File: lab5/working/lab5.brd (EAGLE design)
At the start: 133.9 x 134 mm, 52 parts, among them J1 ISP, Q1 FET, Q2 FET, Q3 FET, Q4 FET, U1 ATMEGA128RFA1, Y1 16MHz

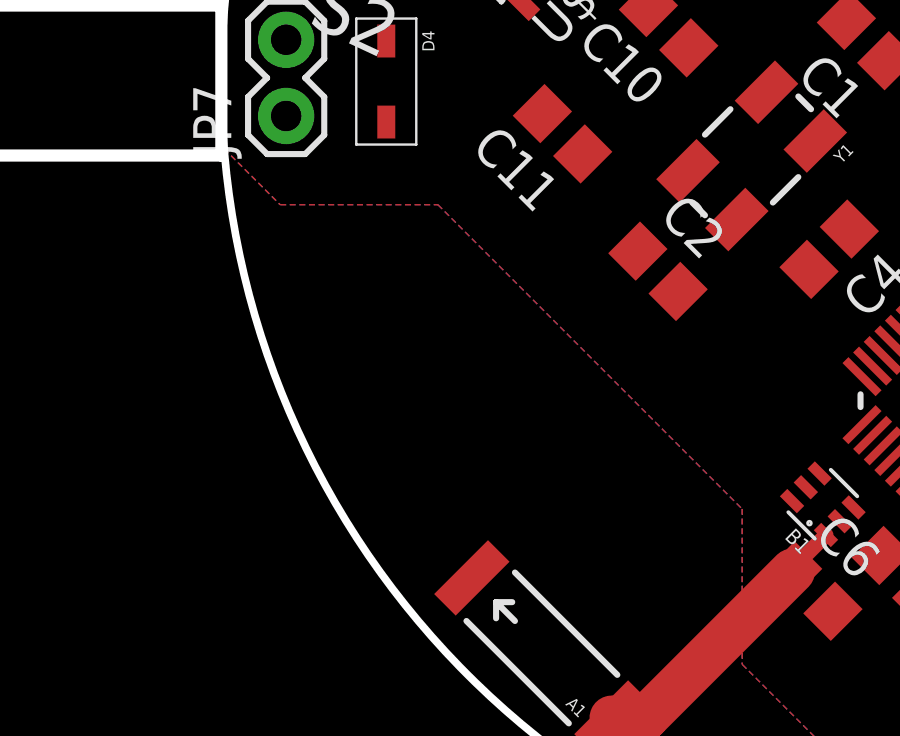
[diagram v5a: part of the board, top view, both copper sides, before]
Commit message: added logo to board
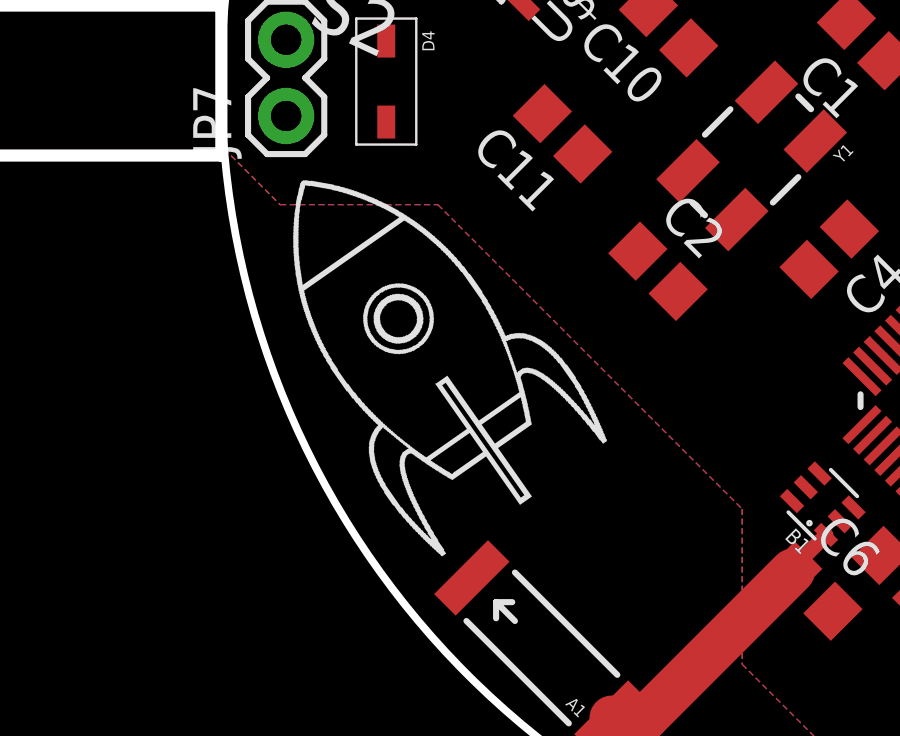
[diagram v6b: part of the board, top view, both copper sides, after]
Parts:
- added U$3: (no value), lab4:ROCKET_LOGO
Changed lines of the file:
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@@
 </element>
 <element name="C5" library="Lab5" package="C0805" value="1 uF" x="9.12498125" y="-7.389125" rot="R135"/>
+<element name="U$3" library="lab4" package="ROCKET_LOGO" value="" x="-20.88895625" y="-16.123996875" rot="R35"/>
 </elements>
 <signals>

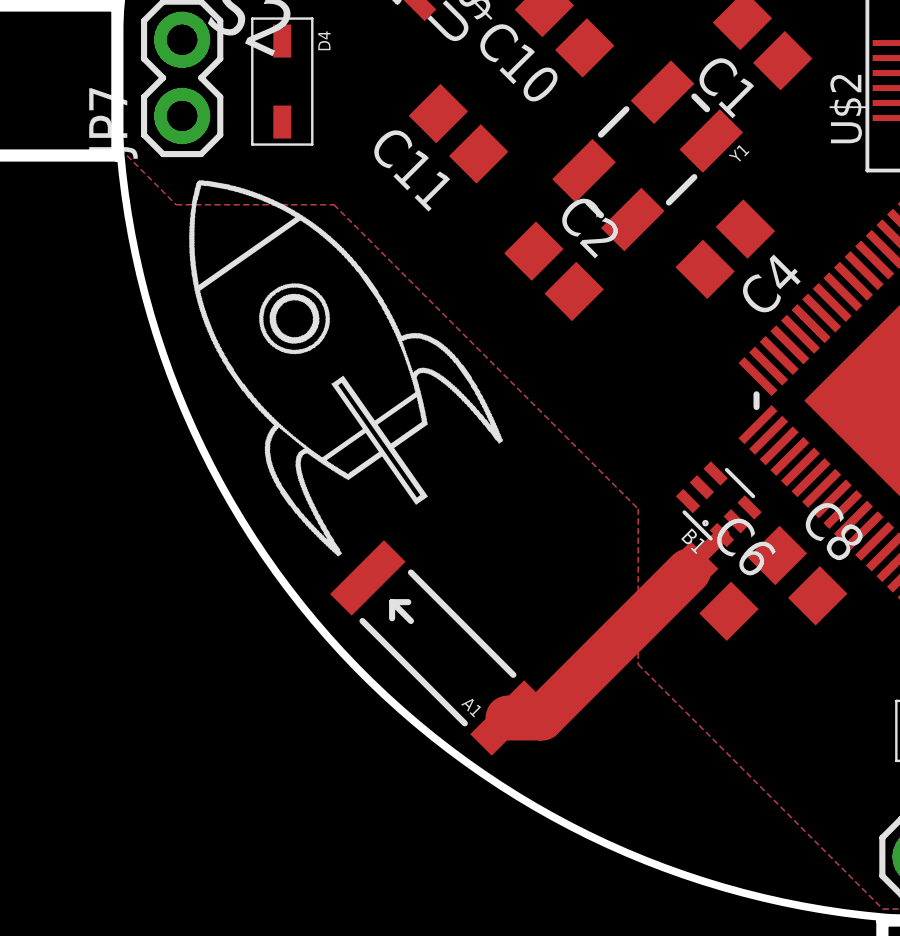
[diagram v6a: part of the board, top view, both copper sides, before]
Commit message: updated radio, moved antenna closer
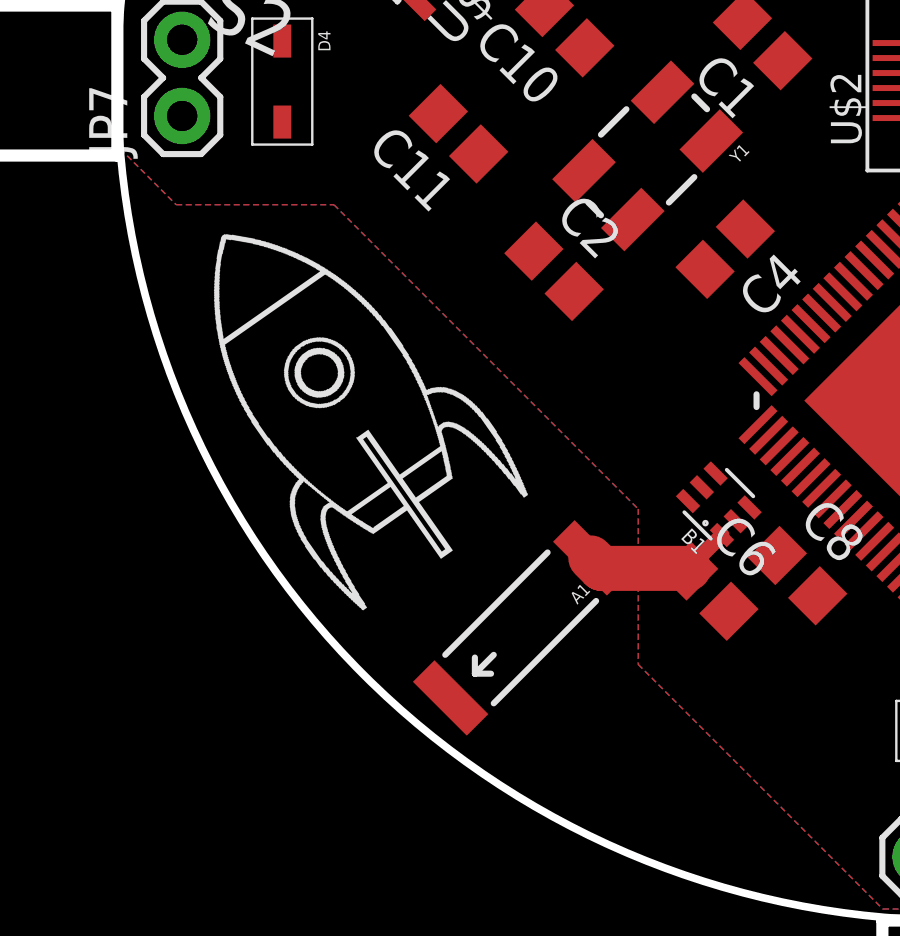
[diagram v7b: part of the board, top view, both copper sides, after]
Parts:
- moved A1 2.84 mm to (-14.6, -18.2), turned to 225 degrees
- moved U$3 1.98 mm to (-20.1, -17.9)
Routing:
- net N$4: track 9.71 -> 5.07 mm
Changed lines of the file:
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@@
 </polygon>
 <wire x1="66.72900625" y1="-0.255303125" x2="66.72900625" y2="0.244696875" width="0.4064" layer="20"/>
+<rectangle x1="-1.32" y1="-1.44" x2="1.32" y2="1.38" layer="41"/>
+<rectangle x1="-1.26" y1="-1.44" x2="1.32" y2="1.38" layer="42"/>
+<rectangle x1="-1.2" y1="-1.32" x2="1.32" y2="1.38" layer="43"/>
+<wire x1="-26.89" y1="-4.53" x2="-21.39" y2="-4.53" width="0.4" layer="39"/>
+<wire x1="-21.39" y1="-4.53" x2="-12.28" y2="-13.64" width="0.4" layer="39"/>
+<wire x1="-12.28" y1="-13.64" x2="-12.44" y2="-13.64" width="0.4" layer="39"/>
+<wire x1="-12.44" y1="-13.64" x2="-18.52" y2="-19.72" width="0.4" layer="39"/>
+<wire x1="-18.52" y1="-19.72" x2="-22.7" y2="-15.54" width="0.4" layer="39"/>
+<wire x1="-22.7" y1="-15.54" x2="-22.7" y2="-13.87" width="0.4" layer="39"/>
+<wire x1="-22.7" y1="-13.87" x2="-24.91" y2="-11.66" width="0.4" layer="39"/>
+<wire x1="-24.91" y1="-11.66" x2="-24.91" y2="-7.56" width="0.4" layer="39"/>
+<wire x1="-24.91" y1="-7.56" x2="-26.89" y2="-5.58" width="0.4" layer="39"/>
+<wire x1="-26.89" y1="-5.58" x2="-26.89" y2="-4.46" width="0.4" layer="39"/>
+<wire x1="-26.89" y1="-4.46" x2="-26.93" y2="-4.42" width="0.4" layer="39"/>
+<wire x1="-26.93" y1="-4.42" x2="-27" y2="-4.42" width="0.4" layer="39"/>
+<wire x1="-11.78" y1="-18.02" x2="-15.53" y2="-21.77" width="0.4" layer="39"/>
+<wire x1="-15.53" y1="-21.77" x2="-15.53" y2="-22.01" width="0.4" layer="39"/>
+<wire x1="-15.53" y1="-22.01" x2="-13.21" y2="-24.33" width="0.4" layer="39"/>
+<wire x1="-13.21" y1="-24.33" x2="-12.44" y2="-24.33" width="0.4" layer="39"/>
+<wire x1="-12.44" y1="-24.33" x2="-11.78" y2="-24.99" width="0.4" layer="39"/>
+<wire x1="-11.78" y1="-24.99" x2="-10.03" y2="-24.99" width="0.4" layer="39"/>
+<wire x1="-10.03" y1="-24.99" x2="-8.91" y2="-26.11" width="0.4" layer="39"/>
+<wire x1="-8.91" y1="-26.11" x2="-7.28" y2="-26.11" width="0.4" layer="39"/>
+<wire x1="-7.28" y1="-26.11" x2="-7.08" y2="-26.31" width="0.4" layer="39"/>
+<wire x1="-7.08" y1="-26.31" x2="-4.53" y2="-26.31" width="0.4" layer="39"/>
+<wire x1="-4.53" y1="-26.31" x2="-11.78" y2="-19.06" width="0.4" layer="39"/>
+<wire x1="-11.78" y1="-19.06" x2="-11.78" y2="-17.94" width="0.4" layer="39"/>
+<wire x1="-26.89" y1="-4.46" x2="-25.26" y2="-6.09" width="0.4" layer="40"/>
+<wire x1="-25.26" y1="-6.09" x2="-25.26" y2="-11" width="0.4" layer="40"/>
+<wire x1="-25.26" y1="-11" x2="-21.46" y2="-14.8" width="0.4" layer="40"/>
+<wire x1="-21.46" y1="-14.8" x2="-21.46" y2="-16.47" width="0.4" layer="40"/>
+<wire x1="-21.46" y1="-16.47" x2="-18.64" y2="-19.29" width="0.4" layer="40"/>
+<wire x1="-18.64" y1="-19.29" x2="-18.32" y2="-19.29" width="0.4" layer="40"/>
+<wire x1="-18.32" y1="-19.29" x2="-12.67" y2="-13.64" width="0.4" layer="40"/>
+<wire x1="-12.67" y1="-13.64" x2="-12.67" y2="-13.17" width="0.4" layer="40"/>
+<wire x1="-12.67" y1="-13.17" x2="-21.27" y2="-4.57" width="0.4" layer="40"/>
+<wire x1="-21.27" y1="-4.57" x2="-27.04" y2="-4.57" width="0.4" layer="40"/>
+<wire x1="-27.04" y1="-4.57" x2="-26.93" y2="-4.46" width="0.4" layer="40"/>
+<wire x1="-26.93" y1="-4.46" x2="-26.92" y2="-4.46" width="0.4" layer="40"/>
+<wire x1="-11.82" y1="-19.17" x2="-4.65" y2="-26.34" width="0.4" layer="40"/>
+<wire x1="-4.65" y1="-26.34" x2="-4.65" y2="-26.58" width="0.4" layer="40"/>
+<wire x1="-4.65" y1="-26.58" x2="-4.88" y2="-26.81" width="0.4" layer="40"/>
+<wire x1="-4.88" y1="-26.81" x2="-6.55" y2="-26.81" width="0.4" layer="40"/>
+<wire x1="-6.55" y1="-26.81" x2="-8.37" y2="-24.99" width="0.4" layer="40"/>
+<wire x1="-8.37" y1="-24.99" x2="-11.54" y2="-24.99" width="0.4" layer="40"/>
+<wire x1="-11.54" y1="-24.99" x2="-13.44" y2="-23.09" width="0.4" layer="40"/>
+<wire x1="-13.44" y1="-23.09" x2="-14.45" y2="-23.09" width="0.4" layer="40"/>
+<wire x1="-14.45" y1="-23.09" x2="-15.61" y2="-21.93" width="0.4" layer="40"/>
+<wire x1="-15.61" y1="-21.93" x2="-15.61" y2="-21.81" width="0.4" layer="40"/>
+<wire x1="-15.61" y1="-21.81" x2="-11.85" y2="-18.05" width="0.4" layer="40"/>
+<wire x1="-11.85" y1="-18.05" x2="-11.85" y2="-17.98" width="0.4" layer="40"/>
+<wire x1="-11.85" y1="-18.05" x2="-11.85" y2="-19.14" width="0.4" layer="40"/>
+<wire x1="-11.85" y1="-19.14" x2="-11.82" y2="-19.17" width="0.4" layer="40"/>
+<wire x1="-11.82" y1="-19.17" x2="-11.82" y2="-19.18" width="0.4" layer="40"/>
 </plain>
 <attributes>
@@
 <classes>
 <class number="0" name="default" width="0" drill="0">
+</class>
+<class number="1" name="RFSIG" width="0.4572" drill="0">
+</class>
+<class number="2" name="HIGHCURRENT" width="0.4572" drill="0">
 </class>
 </classes>
@@
 <element name="C6" library="Lab5" package="C0805" value="0.75F" x="-8.28616875" y="-17.01966875" rot="R315"/>
 <element name="C8" library="Lab5" package="C0805" value="22pF" x="-5.326978125" y="-16.50348125" rot="R315"/>
-<element name="A1" library="Lab5" package="ANTENNA-CHIP5" value="ANTENNA2SMD5" x="-17.315628125" y="-18.91368125" rot="R135"/>
+<element name="A1" library="Lab5" package="ANTENNA-CHIP5" value="ANTENNA2SMD5" x="-14.55631875" y="-18.245628125" rot="R225"/>
 <element name="LED1" library="Lab5" package="CHIP-LED0805" value="GREEN" x="21.018515625" y="-5.39508125" rot="R165"/>
 <element name="LED2" library="Lab5" package="CHIP-LED0805" value="GREEN" x="24.447984375" y="-6.70323125" rot="R165"/>
@@
 </element>
 <element name="C5" library="Lab5" package="C0805" value="1 uF" x="9.12498125" y="-7.389125" rot="R135"/>
-<element name="U$3" library="lab4" package="ROCKET_LOGO" value="" x="-20.88895625" y="-16.123996875" rot="R35"/>
+<element name="U$3" library="lab4" package="ROCKET_LOGO" value="" x="-20.05895625" y="-17.923996875" rot="R35"/>
 </elements>
 <signals>
@@
 <wire x1="-7.386215625" y1="-14.69028125" x2="-5.998728125" y2="-15.831728125" width="0" layer="19" extent="1-1"/>
 </signal>
-<signal name="N$4">
+<signal name="N$4" class="1">
 <contactref element="B1" pad="1"/>
 <contactref element="C6" pad="1"/>
 <contactref element="A1" pad="FEED"/>
+<wire x1="-8.95791875" y1="-16.261984375" x2="-8.95791875" y2="-16.347915625" width="0.5" layer="1"/>
 <wire x1="-7.845834375" y1="-15.1499" x2="-8.95791875" y2="-16.261984375" width="0.5" layer="1"/>
-<wire x1="-8.95791875" y1="-16.261984375" x2="-8.95791875" y2="-16.347915625" width="0.5" layer="1"/>
-<wire x1="-8.95791875" y1="-16.347915625" x2="-13.85855" y2="-21.248546875" width="1.5" layer="1"/>
-<wire x1="-13.85855" y1="-21.248546875" x2="-14.980759375" y2="-21.248546875" width="1.5" layer="1"/>
+<wire x1="-8.95791875" y1="-16.261984375" x2="-11.870225" y2="-16.261984375" width="1.5" layer="1"/>
+<wire x1="-11.870225" y1="-16.261984375" x2="-12.22145" y2="-15.910759375" width="1.5" layer="1"/>
 </signal>
 <signal name="N$8">
@@
 <wire x1="-22.108246875" y1="10.845453125" x2="-17.860340625" y2="9.6036125" width="0" layer="19" extent="1-1"/>
 </signal>
-<signal name="VBAT">
+<signal name="VBAT" class="2">
 <contactref element="S2" pad="1"/>
 <contactref element="U$1" pad="1"/>
@@
 <wire x1="-1.25" y1="-2.15" x2="-5.837396875" y2="10.132971875" width="0" layer="19" extent="1-1"/>
 </signal>
-<signal name="N$16">
+<signal name="N$16" class="2">
 <contactref element="JP7" pad="1"/>
 <contactref element="Q1" pad="P$3"/>
@@
 <wire x1="4.645928125" y1="-20.194821875" x2="4.938909375" y2="-25.46276875" width="0" layer="19" extent="1-1"/>
 </signal>
-<signal name="N$3">
+<signal name="N$3" class="2">
 <contactref element="Q2" pad="P$3"/>
 <contactref element="D1" pad="P$2"/>
@@
 <wire x1="-1.263965625" y1="25.556546875" x2="-1.3109125" y2="22.455628125" width="0" layer="19" extent="1-1"/>
 </signal>
-<signal name="N$12">
+<signal name="N$12" class="2">
 <contactref element="JP4" pad="1"/>
 <contactref element="D3" pad="P$2"/>
@@
 <wire x1="1.309328125" y1="-25.876715625" x2="1.415384375" y2="-21.679015625" width="0" layer="19" extent="1-1"/>
 </signal>
-<signal name="N$15">
+<signal name="N$15" class="2">
 <contactref element="Q3" pad="P$3"/>
 <contactref element="D2" pad="P$2"/>

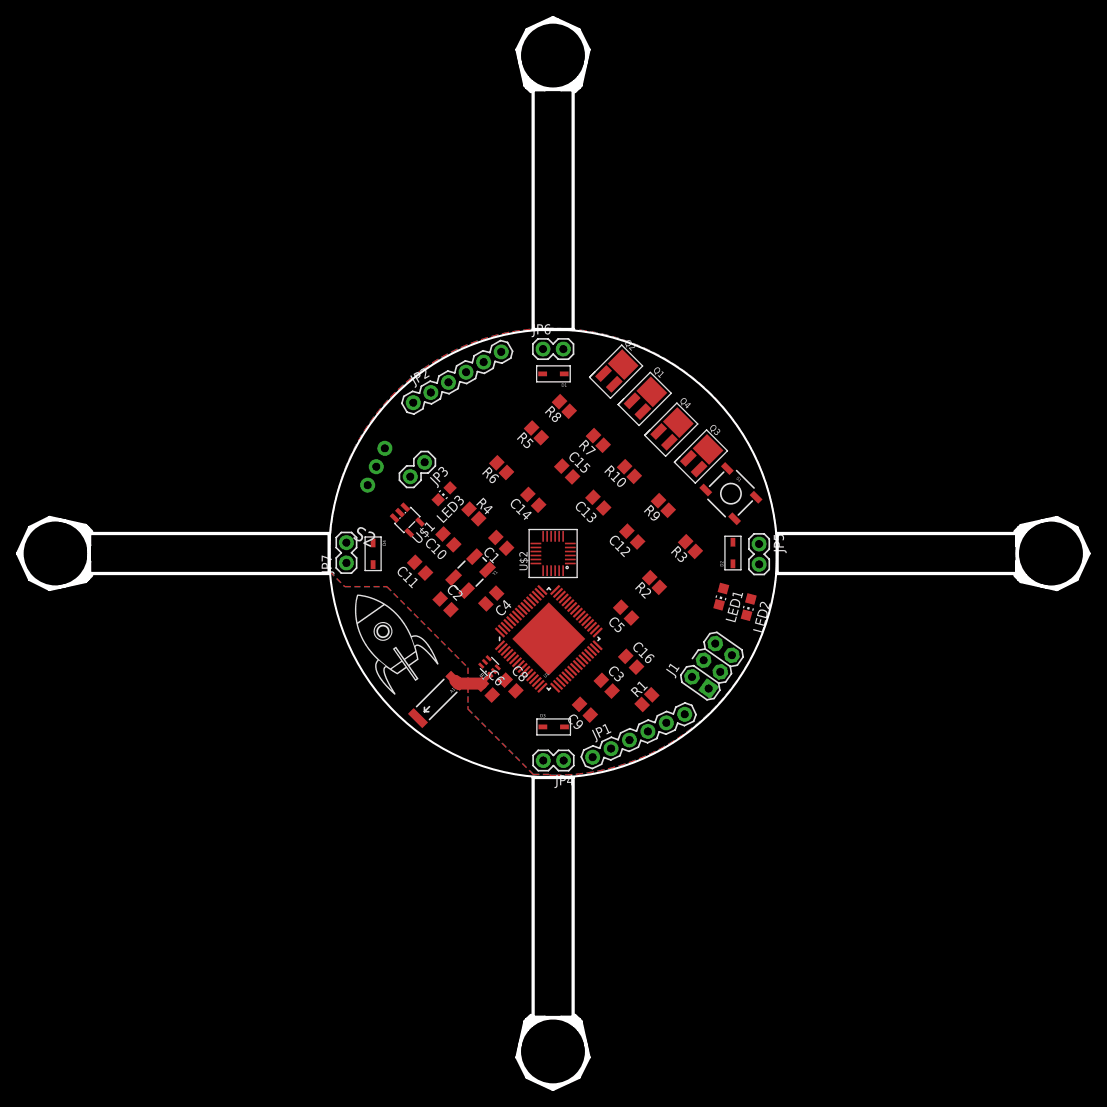
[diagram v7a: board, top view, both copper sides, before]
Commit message: fixed board outline
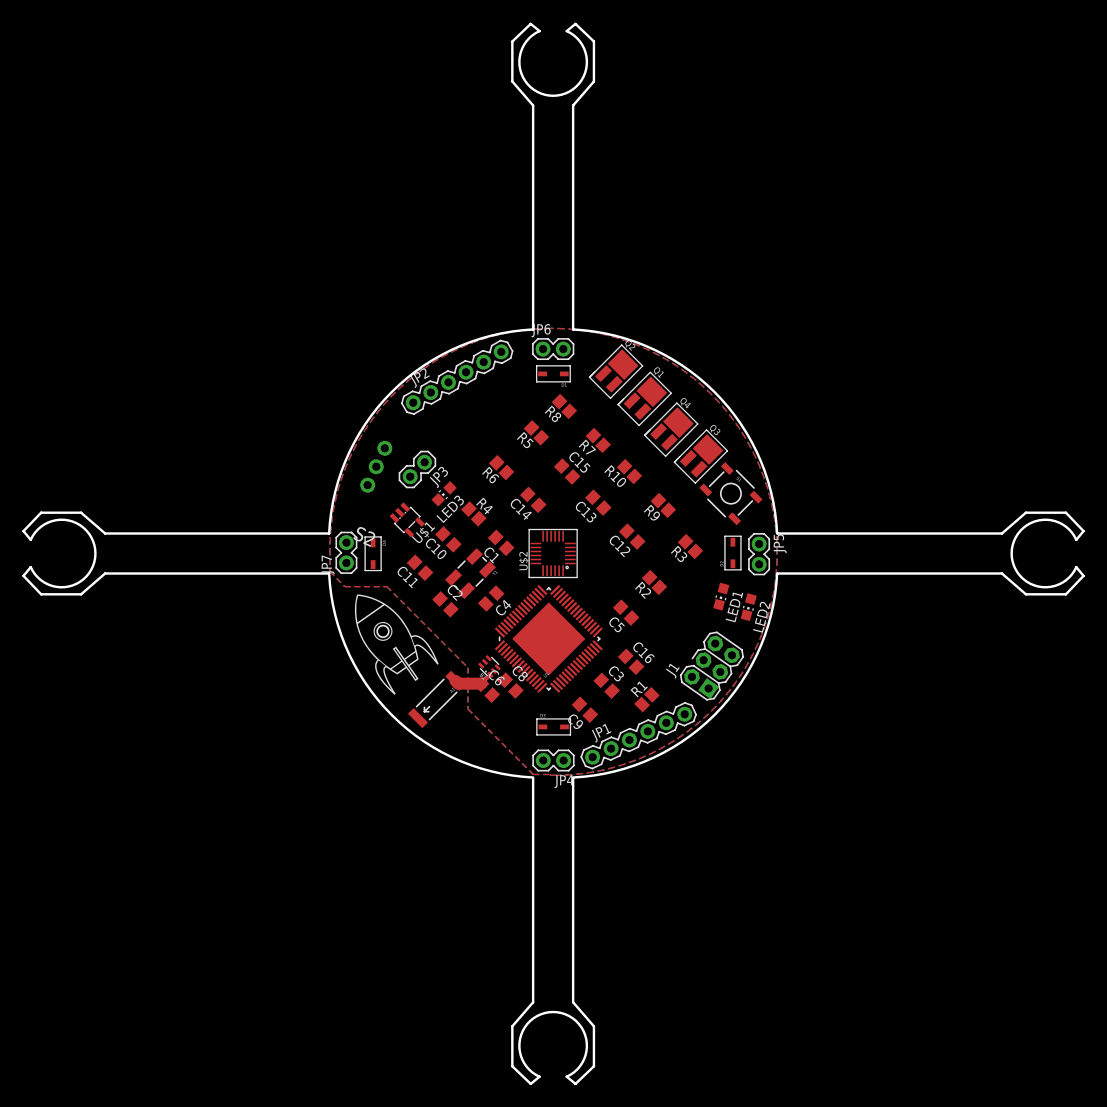
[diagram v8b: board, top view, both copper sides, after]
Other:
- board size 133.9 x 134 mm -> 132.5 x 132.5 mm
